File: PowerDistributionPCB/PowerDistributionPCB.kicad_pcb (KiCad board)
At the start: 4 copper layers, 68 parts, among them J1 USB3_A, K1 RT314F05(gen), K2 RT314F05(gen), K3 RT314F05(gen), K4 RT314F05(gen), Q1 AOD4185, Q10 MMBT2222A, Q11 MMBT2222A, Q12 MMBT2222A, Q2 MMBT2222A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

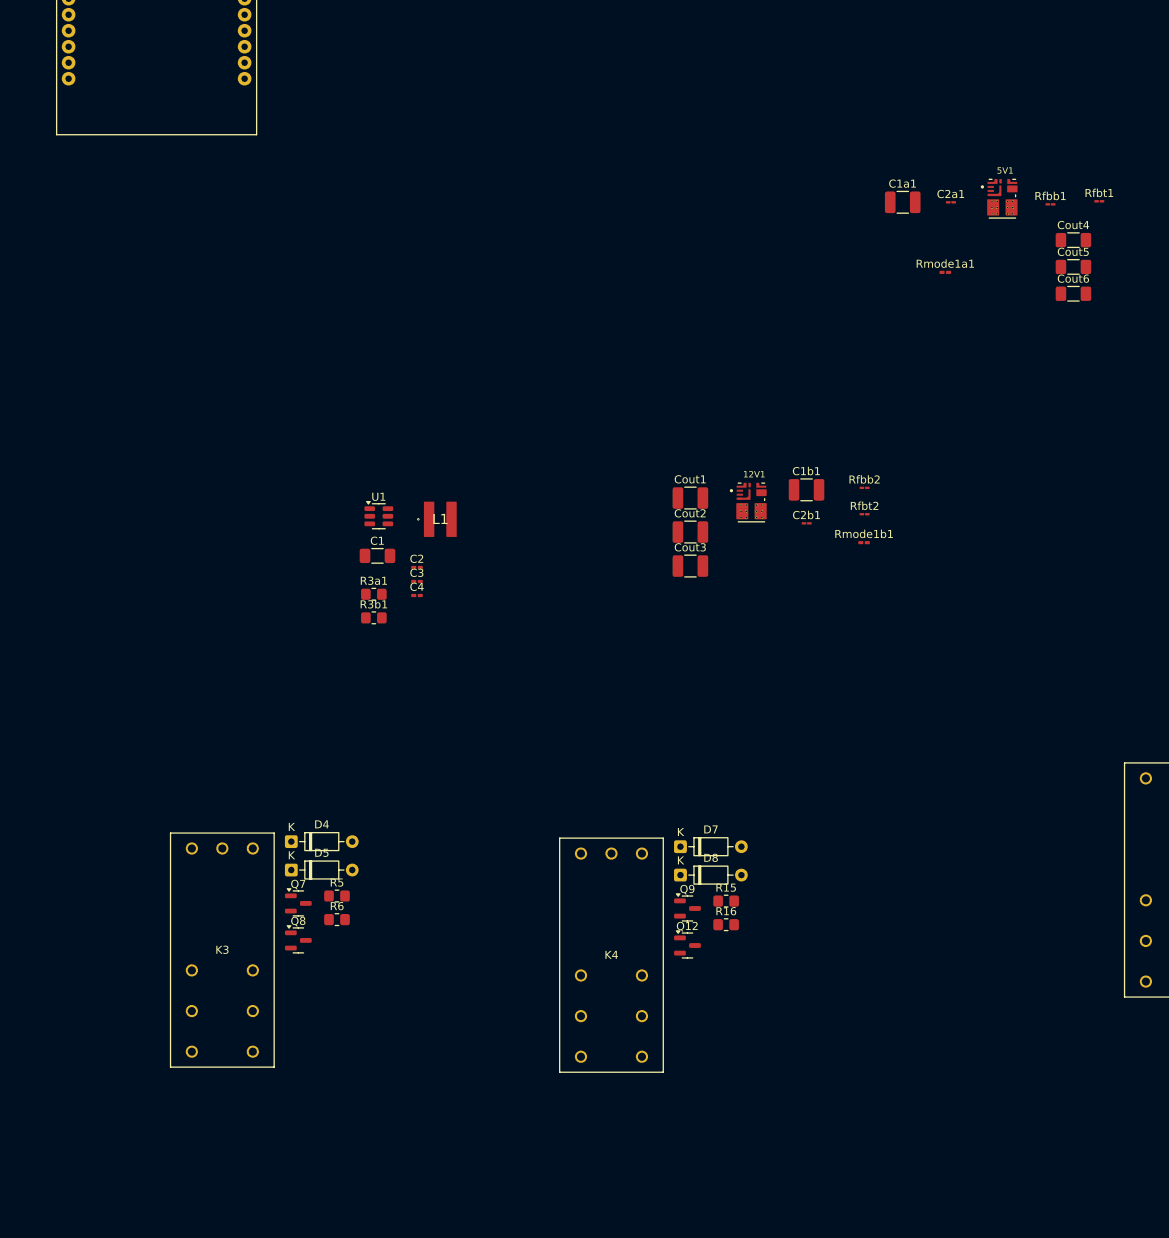
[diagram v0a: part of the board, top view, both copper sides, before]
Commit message: fixed buck converter footprint
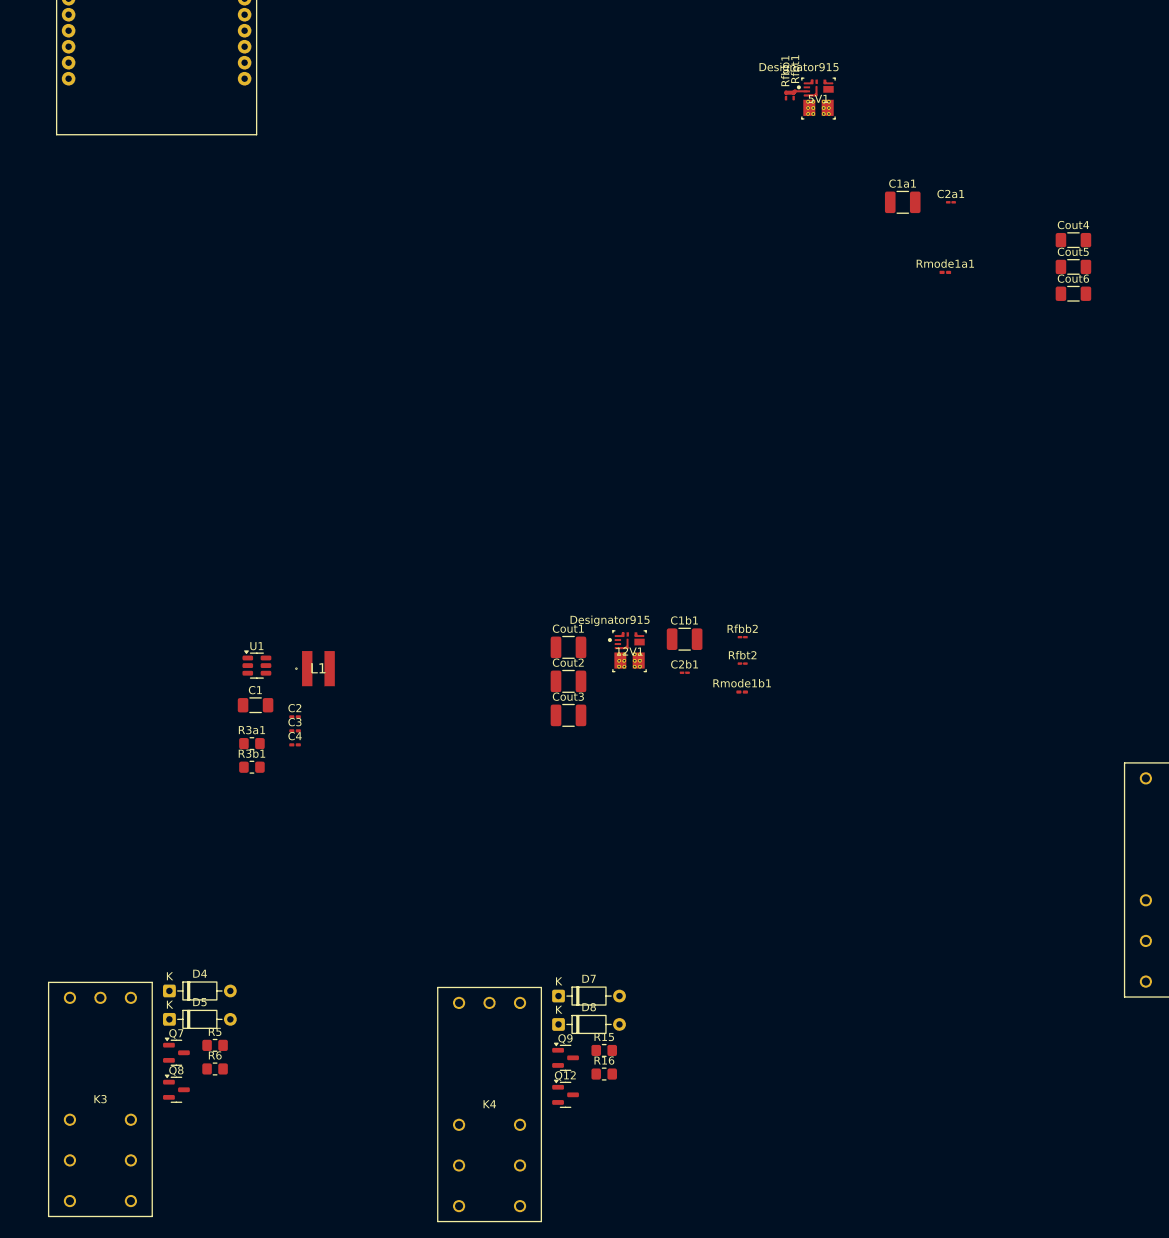
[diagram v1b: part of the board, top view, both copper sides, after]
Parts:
- 12V1, 5V1: footprint CUSail:TPSM84338RCJR -> CUSail:buck_correct
- moved Rfbt1 40.4 mm to (166.7, 49.8), turned to 90 degrees
- moved Rfbb1 35.8 mm to (165.7, 49.8), turned to -90 degrees
- moved 5V1 26.1 mm to (169.8, 50.2)
- moved Cout1 24.1 mm to (138.5, 118.8)
- moved Cout2 24.1 mm to (138.5, 123.0)
- moved Cout3 24.1 mm to (138.5, 127.3)
- moved D7 24.1 mm to (137.3, 162.3)
- moved D8 24.1 mm to (137.3, 165.9)
- moved Q7 24.1 mm to (89.5, 169.4)
- moved Q8 24.1 mm to (89.5, 174.1)
- moved R15 24.1 mm to (143.0, 169.1)
- moved R16 24.1 mm to (143.0, 172.1)
- moved U1 24.1 mm to (99.6, 121.0)
- moved 12V1 24.1 mm to (146.1, 119.3)
- moved C1b1 24.1 mm to (153.0, 117.7)
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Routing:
- net Net-(5V1-FB): track 0.00 -> 2.94 mm

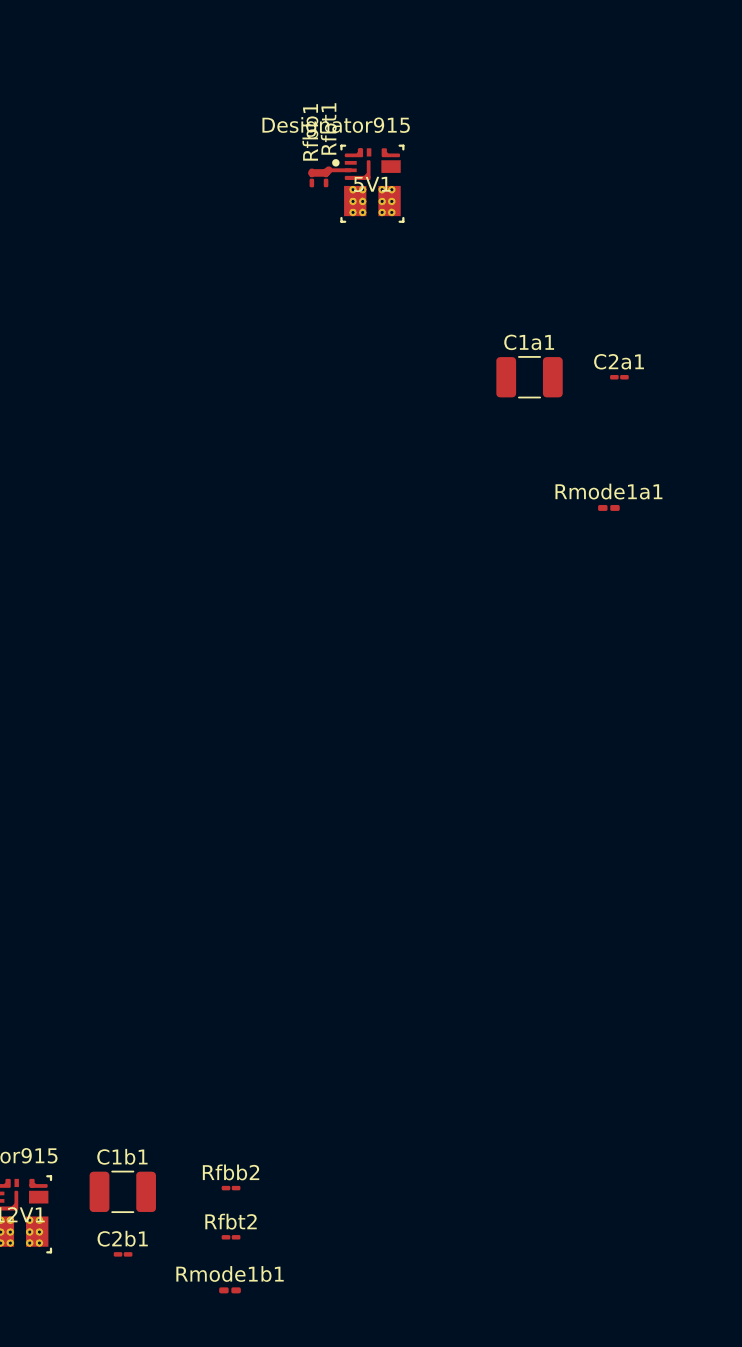
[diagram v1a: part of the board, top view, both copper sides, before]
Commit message: updated layout for new components
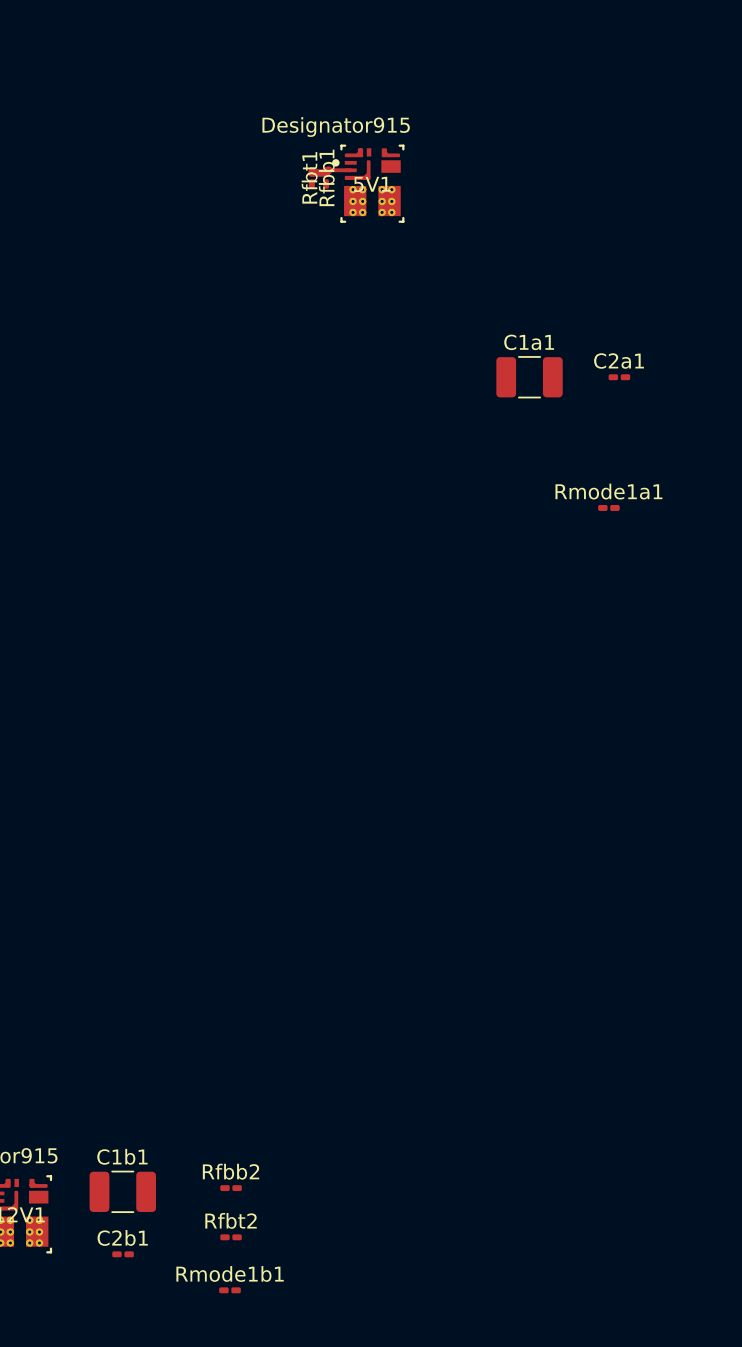
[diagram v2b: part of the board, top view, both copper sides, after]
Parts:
- C2a1, C2b1: footprint Capacitor_SMD:C_01005_0402Metric_Pad0.57x0.30mm_HandSolder -> Capacitor_SMD:C_0201_0603Metric_Pad0.64x0.40mm_HandSolder
- Rfbb1, Rfbb2, Rfbt1, Rfbt2: footprint Capacitor_SMD:C_01005_0402Metric_Pad0.57x0.30mm_HandSolder -> Resistor_SMD:R_0201_0603Metric_Pad0.64x0.40mm_HandSolder

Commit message: started 5V layout
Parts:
- moved C2b1 61.3 mm to (110.6, 77.6)
- moved Cout1 61.3 mm to (96.1, 74.5)
- moved Cout2 61.3 mm to (96.1, 78.7)
- moved Cout3 61.3 mm to (96.1, 83.0)
- moved Rfbb2 61.3 mm to (117.9, 73.2)
- moved Rfbt2 61.3 mm to (117.9, 76.5)
- moved 12V1 61.3 mm to (103.7, 75.0)
- moved C1b1 61.3 mm to (110.6, 73.4)
- moved Rmode1b1 61.3 mm to (117.8, 80.0)
- moved Cout6 45.5 mm to (159.0, 58.6), turned to 180 degrees
- moved Cout5 43.8 mm to (159.0, 61.1), turned to 180 degrees
- moved Cout4 42.8 mm to (159.1, 63.5), turned to 180 degrees
- moved C2a1 30.0 mm to (156.7, 67.7), turned to 90 degrees
- moved Rmode1a1 26.7 mm to (159.0, 70.0)
- moved C1a1 26.1 mm to (154.6, 67.8), turned to 90 degrees
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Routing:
- net GND: track 0.00 -> 23.9 mm, vias 0 -> 3
- net 5VBuck: track 0.00 -> 9.47 mm
- net Sys_Vin: track 0.00 -> 3.77 mm
- net Net-(5V1-MODE): track 0.00 -> 1.12 mm
- net (no net): vias 0 -> 4
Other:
- board text added: "want to add .1 µF decoupling caps between VIN & GND"

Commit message: reorganizing layout
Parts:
- moved J1 119.8 mm to (144.6, 125.9)
- moved C3 87.3 mm to (84.8, 44.1)
- moved C4 87.3 mm to (84.8, 45.8)
- moved L1 87.3 mm to (87.7, 36.3)
- moved R3a1 87.3 mm to (79.4, 45.7)
- moved U1 87.3 mm to (80.0, 35.9)
- moved C1 87.3 mm to (79.9, 40.9)
- moved C2 87.3 mm to (84.8, 42.3)
- moved R3b1 87.3 mm to (79.4, 48.6)
- moved D1 60.8 mm to (172.3, 52.0), turned to 180 degrees
- moved 22V_BATT_IN1 60.3 mm to (188.9, 49.5), turned to -90 degrees
- moved Q1 52.5 mm to (172.4, 43.8)
- moved Main_Bulk(electrolytic)1 47.2 mm to (172.2, 38.1)
- moved R1 46.5 mm to (172.4, 54.4), turned to 180 degrees
- moved R2 46.1 mm to (172.4, 56.6), turned to 180 degrees
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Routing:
- net Batt_Vin: track 0.00 -> 10.9 mm
- net Net-(D1-A): track 0.00 -> 8.13 mm
- net Net-(Q1-D): track 0.00 -> 4.34 mm
- net (no net): vias 4 -> 6

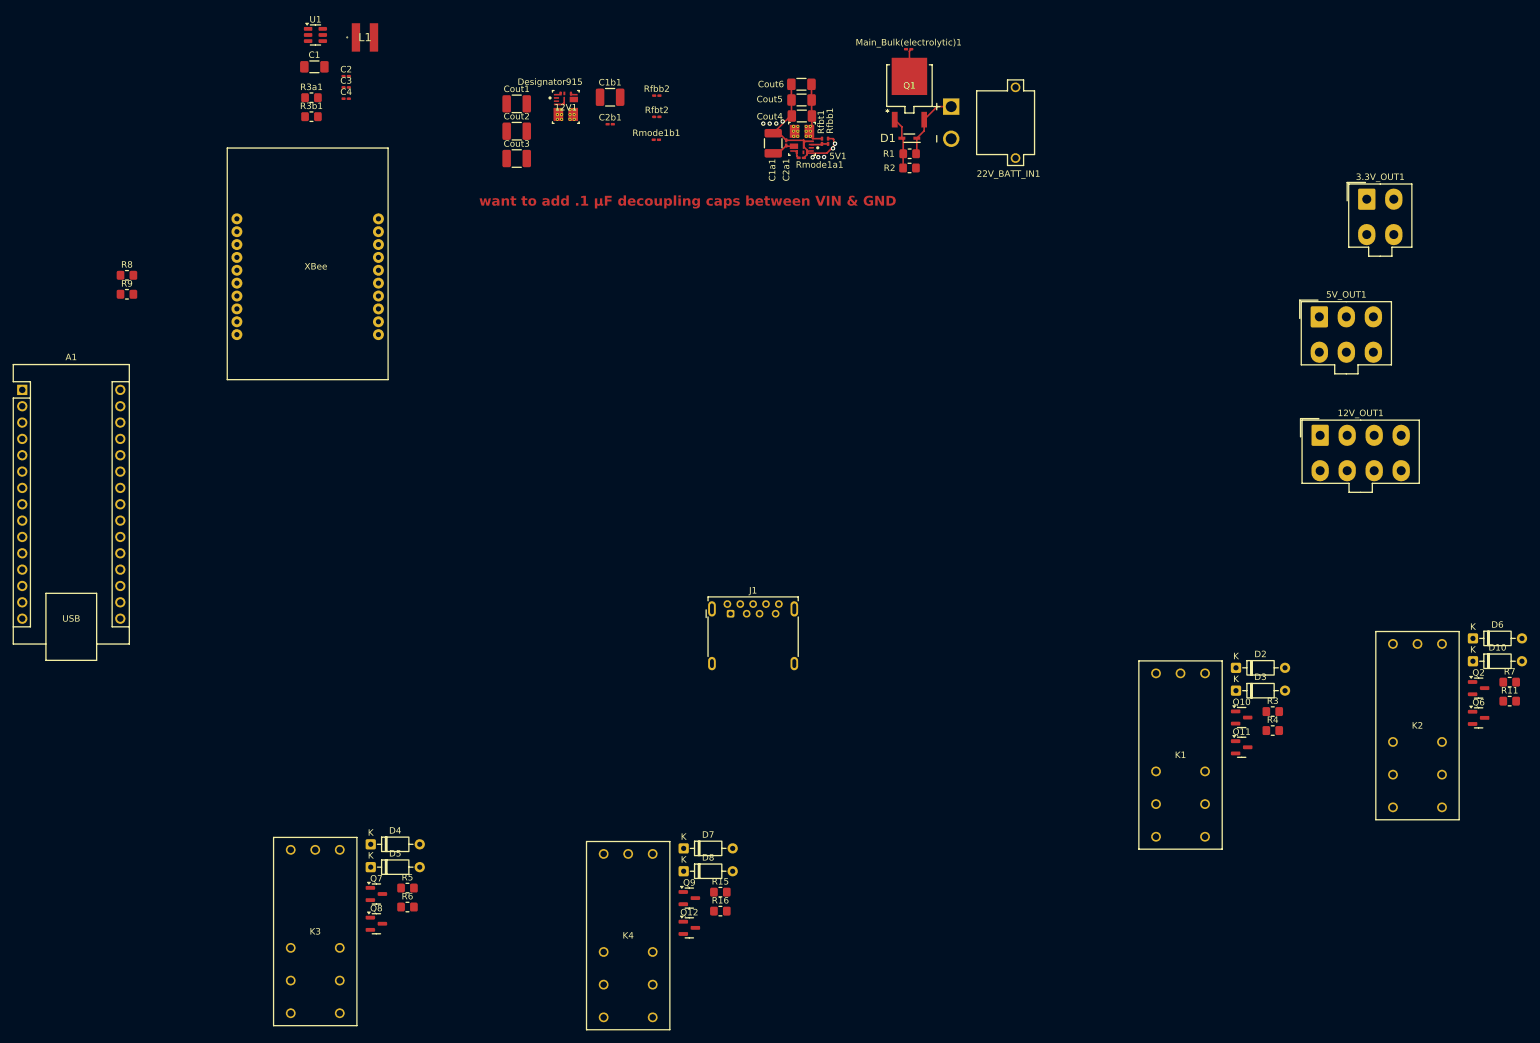
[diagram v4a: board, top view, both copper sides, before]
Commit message: update layout, adjust relay connections/footprint
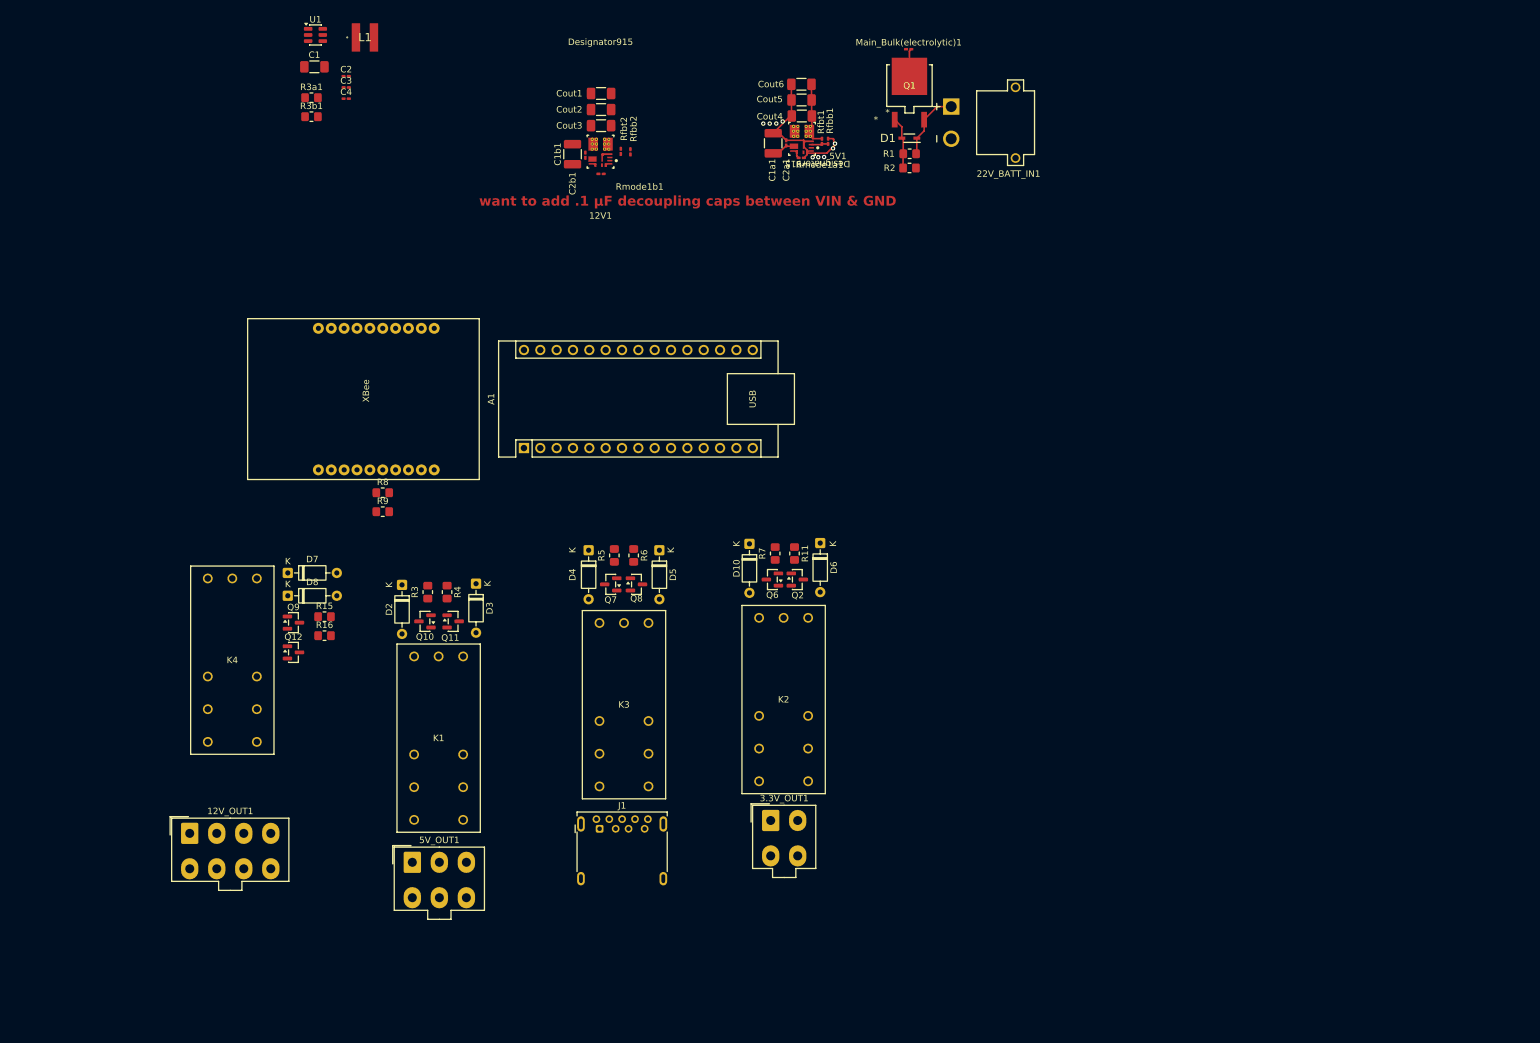
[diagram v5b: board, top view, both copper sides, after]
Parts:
- Cout1, Cout2, Cout3: footprint Capacitor_SMD:C_1210_3225Metric_Pad1.33x2.70mm_HandSolder -> Capacitor_SMD:C_1206_3216Metric_Pad1.33x1.80mm_HandSolder
- moved 12V_OUT1 186.3 mm to (60.5, 160.0)
- moved 5V_OUT1 164.5 mm to (95.1, 164.5)
- moved 3.3V_OUT1 133.8 mm to (150.8, 158.0)
- moved R3 132.6 mm to (97.5, 122.5), turned to -90 degrees
- moved D2 130.3 mm to (93.5, 121.4), turned to -90 degrees
- moved R4 130.1 mm to (100.5, 122.5), turned to -90 degrees
- moved Q10 127.8 mm to (97.1, 127.0), turned to 180 degrees
- moved Q11 124.1 mm to (101.4, 127.0)
- moved D3 119.3 mm to (105.0, 121.2), turned to -90 degrees
- moved R7 115.9 mm to (151.5, 116.5), turned to -90 degrees
- moved K1 115.3 mm to (95.4, 132.5)
- moved D10 113.9 mm to (147.5, 115.0), turned to -90 degrees
- moved R11 113.5 mm to (154.5, 116.5), turned to -90 degrees
- moved Q6 111.9 mm to (151.1, 120.5), turned to 180 degrees
- moved Q2 107.2 mm to (154.9, 120.5)
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
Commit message: general layout on power
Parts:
- moved 22V_BATT_IN1 44.4 mm to (151.5, 73.5)
- moved Main_Bulk(electrolytic)1 44.4 mm to (134.9, 62.1)
- moved Q1 44.4 mm to (135.0, 67.7)
- moved R1 44.4 mm to (135.0, 78.3)
- moved D1 44.4 mm to (135.0, 75.9)
- moved R2 44.4 mm to (135.0, 80.5)
- moved Cout4 38.9 mm to (120.1, 64.2)
- moved Rfbb1 38.9 mm to (124.2, 68.2)
- moved Rmode1a1 38.9 mm to (120.0, 70.7)
- moved C1a1 38.9 mm to (115.6, 68.5)
- moved 5V1 38.9 mm to (120.1, 67.7)
- moved C2a1 38.9 mm to (117.6, 68.4)
- moved Cout5 38.9 mm to (120.0, 61.7)
- moved Cout6 38.9 mm to (120.0, 59.3)
- moved Rfbt1 38.9 mm to (123.2, 68.2)
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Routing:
- net 5VSafe: track 0.00 -> 191.7 mm
- net 12V_ON: track 0.00 -> 53.5 mm
- net 12V_OFF: track 0.00 -> 53.0 mm
- net XbeeTX: track 0.00 -> 48.1 mm
- net 12VRelayOut: track 0.00 -> 43.5 mm
- net XBeeRESET: track 0.00 -> 38.0 mm
- net 5V_ON: track 0.00 -> 35.9 mm
- net 5VRelayOut: track 0.00 -> 35.6 mm
- net 5V_OFF: track 0.00 -> 35.5 mm
- net 3.3VRelayOut: track 0.00 -> 34.3 mm
- net Net-(XBee1-DIN/CONFIG): track 0.00 -> 31.8 mm
- net VN_ON: track 0.00 -> 17.8 mm
- net VN_OFF: track 0.00 -> 17.3 mm
- net 5VBuck: track 9.47 -> 24.7 mm
- net VNRelayOut: track 0.00 -> 14.3 mm
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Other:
- board text added: "want to add .1 µF decoupling caps between VIN & GND we already have them as c2 i think might want to tie clocks of bucks together though?"
- board text removed: "want to add .1 µF decoupling caps between VIN & GND"
